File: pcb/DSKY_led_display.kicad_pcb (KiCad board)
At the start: 4 copper layers, 63.5 x 107.9 mm, 237 parts, among them J1 105133-0001, J2 20021221-00010C4LF, J3 TSM-104-01-L-SV, Q1 BSS138, Q2 BSS138, Q3 BSS138, Q4 BSS138, SW1 SWITCH_TACT_SMT4.6X2.8, U1 AP2204K-3.3, U2 LP5036, U3 LP5036, U4 LP5036, U5 LP5036, U6 ATSAMD21E18A-A, U7 LP5036, U8 LP5036

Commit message: V2 pcb as-ordered for testing
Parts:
- added C10: 1 uF, Capacitor_SMD:C_0603_1608Metric, F.Cu at (89.4, 128.4)
- added C11: 1 uF, Capacitor_SMD:C_0603_1608Metric, F.Cu at (64.1, 41.1)
- added C12: 1 uF, Capacitor_SMD:C_0603_1608Metric, F.Cu at (89.4, 109.0)
- added C13: 1 uF, Capacitor_SMD:C_0603_1608Metric, F.Cu at (43.9, 41.1)
- added C14: 1 uF, Capacitor_SMD:C_0603_1608Metric, F.Cu at (85.7, 41.1)
- added C9: 1 uF, Capacitor_SMD:C_0603_1608Metric, F.Cu at (89.5, 90.2)
- D191, D192: value D_Schottky -> B0540W
- R15, R16, R17, R18, R19, R20: value 3.7K -> 3.65K
- SW1: value SWITCH_TACT_SMT4.6X2.8 -> KMR241NG
- moved R15 57.2 mm to (92.7, 91.7), turned to 0 degrees
- moved C4 56.4 mm to (92.1, 95.5)
- moved C6 49.3 mm to (49.1, 38.1), turned to 0 degrees
- moved R6 45.3 mm to (46.1, 38.1), turned to 0 degrees
- moved R19 45.2 mm to (43.1, 38.1), turned to 180 degrees
- moved U2 43.5 mm to (85.1, 92.7), turned to 270 degrees
- moved U7 38.1 mm to (46.5, 45.6), turned to 0 degrees
- moved Q4 16.6 mm to (50.6, 75.2)
- moved Q3 16.6 mm to (57.0, 75.2)
- moved R11 16.6 mm to (57.1, 78.6)
- moved R13 16.6 mm to (50.6, 78.6)
- moved R14 16.6 mm to (50.6, 71.2)
- moved R12 16.6 mm to (57.0, 71.2)
- moved C3 13.4 mm to (92.3, 116.0), turned to 270 degrees
- moved J2 13.0 mm to (60.7, 53.7)
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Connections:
- U2 pad 45: +5V -> Net-(C9-Pad1)
- U3 pad 45: +5V -> Net-(C10-Pad1)
- U4 pad 45: +5V -> Net-(C12-Pad1)
- U5 pad 45: +5V -> Net-(C11-Pad1)
- U7 pad 45: +5V -> Net-(C13-Pad1)
- U8 pad 45: +5V -> Net-(C14-Pad1)
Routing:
- net GND: track 1070.7 -> 1396.6 mm, vias 9 -> 34
- net abus30: track 7.82 -> 63.9 mm
- net abus31: track 3.65 -> 58.1 mm
- net g5bus3: track 16.9 -> 69.9 mm, vias 1 -> 2
- net g5bus2: track 29.2 -> 79.5 mm, vias 2 -> 3
- net abus34: track 9.21 -> 59.2 mm
- net abus29: track 13.2 -> 60.2 mm
- net g5bus1: track 41.2 -> 88.0 mm, vias 2 -> 3
- net abus32: track 9.44 -> 55.2 mm
- net g6bus2: track 39.3 -> 84.2 mm, vias 1 -> 2
- net /EN0: track 173.9 -> 129.4 mm, vias 5 -> 6
- net g6bus3: track 36.6 -> 79.6 mm
- net abus33: track 11.6 -> 54.6 mm
- net g6bus1: track 51.6 -> 94.1 mm
- net abus0: track 52.5 -> 11.3 mm, vias 2 -> 1
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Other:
- net class Data: clearance 0.1 -> 0.15; trace_width 0.15 -> 0.2
- net class Default: clearance 0.1 -> 0.15; trace_width 0.15 -> 0.2
- net class GND added: clearance 0.15, trace_width 0.2, via_dia 0.6, via_drill 0.3
- net class Power: clearance 0.1 -> 0.15; trace_width 0.15 -> 0.2
- rule trace_clearance: 0.1 -> 0.15
- board text added: "+5V"
- board text added: "DSKY LED Display V2 Riley Rainey 2021-01-22"
- board text added: "GND"
- board text added: "N/C"
- board text added: "https://github.com/rrainey/DSKY-digital-indicator-replica"
- board text removed: "DSKY LED Display V1 Riley Rainey 2021-01-12"

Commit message: V3 board
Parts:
- removed Q1, Q2, Q3, Q4: BSS138, digikey-footprints:SOT-23-3
- removed R13, R14: 10K, Resistor_SMD:R_0603_1608Metric
- removed the REF** at (46.5, 110.7)
- added C15: 10 uF, Capacitor_SMD:C_0603_1608Metric, F.Cu at (52.2, 75.7)
- added REF**: OSHW-Logo2_24.3x20mm_SilkScreen, Symbol:OSHW-Logo2_24.3x20mm_SilkScreen, F.Cu at (48.7, 110.6)
- added U9: TCA9543ADR, Package_SO:SOIC-14_3.9x8.7mm_P1.27mm, F.Cu at (52.4, 81.0)
- J2: value 20021221-00010C4LF -> 3221-10-0300-00-TR
- R10, R7, R8, R9: value 10K -> 1K
- R11, R12: value 10K -> 4.7K
- moved R12 43.3 mm to (83.8, 37.1), turned to 180 degrees
- moved R11 39.6 mm to (93.7, 93.9), turned to 90 degrees
- moved R10 25.1 mm to (59.3, 83.1), turned to 270 degrees
- moved R8 24.3 mm to (46.7, 81.5), turned to 270 degrees
- moved R7 20.2 mm to (45.1, 83.1), turned to 270 degrees
- moved R9 16.1 mm to (57.7, 81.5), turned to 270 degrees
- moved R19 6.56 mm to (49.3, 40.1)
- moved R6 6.10 mm to (52.2, 38.3), turned to 90 degrees
- moved C13 5.40 mm to (49.3, 41.7)
- moved U7 5.33 mm to (51.8, 46.2)
- moved C6 4.66 mm to (53.8, 38.3), turned to 90 degrees
- moved R20 3.68 mm to (82.3, 40.2)
- moved C14 3.49 mm to (82.3, 41.8)
- moved R3 3.40 mm to (90.2, 135.9), turned to 270 degrees
- moved J2 3.28 mm to (60.7, 57.0)
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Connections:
- C1 pad 1: +5V -> VCC
- C2 pad 1: +5V -> VCC
- C3 pad 1: +5V -> VCC
- C4 pad 1: +5V -> VCC
- C6 pad 1: +5V -> VCC
- C7 pad 1: +5V -> VCC
- D191 pad 2: +5V -> VCC
- J3 pad 1: +5V -> VCC
- R1 pad 1: +5V -> VCC
- R10 pad 1: /EN1 -> VCC
- R10 pad 2: +5V -> /SDA1
- R11 pad 1: /3SDA -> VCC
- R11 pad 2: +3V3 -> Net-(R11-Pad2)
- R12 pad 1: /SDA -> VCC
- R12 pad 2: +5V -> Net-(R12-Pad2)
- R2 pad 1: +5V -> VCC
- R3 pad 1: +5V -> VCC
- R6 pad 1: +5V -> VCC
- R7 pad 1: /3EN0 -> VCC
- R7 pad 2: +3V3 -> /SCL0
- R8 pad 1: /EN0 -> VCC
- R8 pad 2: +5V -> /SDA0
- R9 pad 1: /3EN1 -> VCC
- R9 pad 2: +3V3 -> /SCL1
- U2 pad 40: +5V -> VCC
- U2 pad 41: /SDA -> /SDA0
- U2 pad 42: /SCL -> /SCL0
- U2 pad 43: /EN0 -> Net-(R11-Pad2)
- U3 pad 40: +5V -> VCC
- U3 pad 41: /SDA -> /SDA0
- U3 pad 42: /SCL -> /SCL0
- U3 pad 43: /EN0 -> Net-(R3-Pad2)
- U4 pad 40: +5V -> VCC
- U4 pad 41: /SDA -> /SDA0
- U4 pad 42: /SCL -> /SCL0
- U4 pad 43: /EN0 -> Net-(R1-Pad2)
- U5 pad 40: +5V -> VCC
- U5 pad 41: /SDA -> /SDA0
- U5 pad 42: /SCL -> /SCL0
- U5 pad 43: /EN0 -> Net-(R2-Pad2)
- U6 pad 1: /3EN0 -> Net-(U6-Pad1)
- U6 pad 2: /3EN1 -> Net-(U6-Pad2)
- U6 pad 22: /D- -> Net-(U6-Pad22)
- U6 pad 23: /D+ -> /D-
- U6 pad 24: Net-(U6-Pad24) -> /D+
- U6 pad 3: Net-(U6-Pad3) -> /BRESET
- U7 pad 40: +5V -> VCC
- U7 pad 41: /SDA -> /SDA1
- U7 pad 42: /SCL -> /SCL1
- U7 pad 43: /EN1 -> Net-(R6-Pad2)
- U8 pad 40: +5V -> VCC
- U8 pad 41: /SDA -> /SDA1
- U8 pad 42: /SCL -> /SCL1
- U8 pad 43: /EN1 -> Net-(R12-Pad2)
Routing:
- net +5V: track 244.6 -> 0.00 mm, vias 5 -> 0
- net VCC: track 0.00 -> 226.6 mm, vias 0 -> 5
- net /SCL: track 200.0 -> 0.00 mm, vias 7 -> 0
- net /SDA: track 188.3 -> 0.00 mm, vias 7 -> 0
- net GND: track 1396.6 -> 1226.0 mm, vias 34 -> 7
- net /SDA0: track 0.00 -> 139.3 mm, vias 0 -> 5
- net /SCL0: track 0.00 -> 138.4 mm, vias 0 -> 5
- net /EN0: track 129.4 -> 0.00 mm, vias 6 -> 0
- net /SCL1: track 0.00 -> 93.7 mm, vias 0 -> 3
- net /SDA1: track 0.00 -> 88.1 mm, vias 0 -> 3
- net /EN1: track 69.9 -> 0.00 mm, vias 3 -> 0
- net cbus7: track 37.4 -> 14.1 mm, vias 2 -> 1
- net g5bus1: track 88.0 -> 67.9 mm, vias 3 -> 2
- net g5bus0: track 92.9 -> 74.4 mm
- net abus7: track 32.1 -> 13.6 mm, vias 2 -> 1
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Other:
- net class VCC added: clearance 0.15, trace_width 0.45, via_dia 0.6, via_drill 0.3
- board text added: "+3.3V"
- board text added: "DSKY LED Display V3 Riley Rainey 2021-02-23"
- board text removed: "+5V"
- board text removed: "DSKY LED Display V2 Riley Rainey 2021-01-22"

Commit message: V4 board
Version 4 of the PCB
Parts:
- removed R1, R11, R12, R2, R3, R6: 4.7K, Resistor_SMD:R_0603_1608Metric
- added R13: 0K, Resistor_SMD:R_0603_1608Metric, F.Cu at (59.2, 66.5)
- added R14: 1K, Resistor_SMD:R_0603_1608Metric, F.Cu at (59.5, 74.0)
- added R21: 1K, Resistor_SMD:R_0603_1608Metric, F.Cu at (57.8, 74.0)
- added R22: 1K, Resistor_SMD:R_0603_1608Metric, F.Cu at (43.3, 81.5)
- added R23: 1K, Resistor_SMD:R_0603_1608Metric, F.Cu at (59.3, 86.6)
- moved C1 3.71 mm to (90.7, 132.4), turned to 0 degrees
- moved C3 3.55 mm to (90.7, 112.8), turned to 0 degrees
- moved R17 3.53 mm to (91.0, 109.0)
- moved R16 2.69 mm to (91.0, 128.4)
- moved R15 2.61 mm to (91.1, 90.2)
- moved C4 2.46 mm to (90.3, 93.8), turned to 0 degrees
- moved R7 1.60 mm to (45.0, 81.5)
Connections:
- D10 pad 1: GND -> g0bus1
- D10 pad 2: g0bus1 -> VCC
- D100 pad 1: GND -> abus32
- D100 pad 2: abus32 -> VCC
- D101 pad 1: GND -> abus3
- D101 pad 2: abus3 -> VCC
- D102 pad 1: GND -> sabus2
- D102 pad 2: sabus2 -> VCC
- D103 pad 1: GND -> abus10
- D103 pad 2: abus10 -> VCC
- D104 pad 1: GND -> abus17
- D104 pad 2: abus17 -> VCC
- D105 pad 1: GND -> abus24
- D105 pad 2: abus24 -> VCC
- D106 pad 1: GND -> abus31
- D106 pad 2: abus31 -> VCC
- D107 pad 1: GND -> g5bus0
- D107 pad 2: g5bus0 -> VCC
- D108 pad 1: GND -> g5bus1
- D108 pad 2: g5bus1 -> VCC
- D109 pad 1: GND -> g5bus2
- D109 pad 2: g5bus2 -> VCC
- D11 pad 1: GND -> g0bus6
- D11 pad 2: g0bus6 -> VCC
- D110 pad 1: GND -> g5bus3
- D110 pad 2: g5bus3 -> VCC
- D111 pad 1: GND -> bbus0
- D111 pad 2: bbus0 -> VCC
- D112 pad 1: GND -> sbbus0
- D112 pad 2: sbbus0 -> VCC
- D113 pad 1: GND -> bbus7
- D113 pad 2: bbus7 -> VCC
- D114 pad 1: GND -> bbus14
- D114 pad 2: bbus14 -> VCC
- D115 pad 1: GND -> bbus21
- D115 pad 2: bbus21 -> VCC
- D116 pad 1: GND -> bbus28
- D116 pad 2: bbus28 -> VCC
- D117 pad 1: GND -> bbus5
- D117 pad 2: bbus5 -> VCC
- D118 pad 1: GND -> bbus1
- D118 pad 2: bbus1 -> VCC
- D119 pad 1: GND -> bbus12
- D119 pad 2: bbus12 -> VCC
- D12 pad 1: GND -> g0bus5
- D12 pad 2: g0bus5 -> VCC
- D120 pad 1: GND -> bbus19
- D120 pad 2: bbus19 -> VCC
- D121 pad 1: GND -> bbus8
- D121 pad 2: bbus8 -> VCC
- D122 pad 1: GND -> bbus15
- D122 pad 2: bbus15 -> VCC
- D123 pad 1: GND -> bbus26
- D123 pad 2: bbus26 -> VCC
- D124 pad 1: GND -> bbus33
- D124 pad 2: bbus33 -> VCC
- D125 pad 1: GND -> bbus22
- D125 pad 2: bbus22 -> VCC
- D126 pad 1: GND -> bbus29
- D126 pad 2: bbus29 -> VCC
- D127 pad 1: GND -> sbbus1
- D127 pad 2: sbbus1 -> VCC
- D128 pad 1: GND -> bbus6
- D128 pad 2: bbus6 -> VCC
- D129 pad 1: GND -> bbus13
- D129 pad 2: bbus13 -> VCC
- D13 pad 1: GND -> g0bus4
- D13 pad 2: g0bus4 -> VCC
- D130 pad 1: GND -> bbus20
- D130 pad 2: bbus20 -> VCC
- D131 pad 1: GND -> bbus27
- D131 pad 2: bbus27 -> VCC
- D132 pad 1: GND -> bbus34
- D132 pad 2: bbus34 -> VCC
- D133 pad 1: GND -> bbus2
- D133 pad 2: bbus2 -> VCC
- D134 pad 1: GND -> bbus4
- D134 pad 2: bbus4 -> VCC
- D135 pad 1: GND -> bbus9
- D135 pad 2: bbus9 -> VCC
- D136 pad 1: GND -> bbus16
- D136 pad 2: bbus16 -> VCC
- D137 pad 1: GND -> bbus11
- D137 pad 2: bbus11 -> VCC
- D138 pad 1: GND -> bbus18
- D138 pad 2: bbus18 -> VCC
- D139 pad 1: GND -> bbus23
- D139 pad 2: bbus23 -> VCC
- D14 pad 1: GND -> g0bus7
- D14 pad 2: g0bus7 -> VCC
- D140 pad 1: GND -> bbus30
- D140 pad 2: bbus30 -> VCC
- D141 pad 1: GND -> bbus25
- D141 pad 2: bbus25 -> VCC
- D142 pad 1: GND -> bbus32
- D142 pad 2: bbus32 -> VCC
- D143 pad 1: GND -> sbbus2
- D143 pad 2: sbbus2 -> VCC
- D144 pad 1: GND -> bbus3
- D144 pad 2: bbus3 -> VCC
- D145 pad 1: GND -> bbus10
- D145 pad 2: bbus10 -> VCC
- D146 pad 1: GND -> bbus17
- D146 pad 2: bbus17 -> VCC
- D147 pad 1: GND -> bbus24
- D147 pad 2: bbus24 -> VCC
- D148 pad 1: GND -> bbus31
- D148 pad 2: bbus31 -> VCC
- D149 pad 1: GND -> g6bus0
- D149 pad 2: g6bus0 -> VCC
- D15 pad 1: GND -> dbus0
- D15 pad 2: dbus0 -> VCC
- D150 pad 1: GND -> g6bus1
- D150 pad 2: g6bus1 -> VCC
- D151 pad 1: GND -> g6bus2
- D151 pad 2: g6bus2 -> VCC
- D152 pad 1: GND -> g6bus3
- D152 pad 2: g6bus3 -> VCC
- D153 pad 1: GND -> scbus0
- D153 pad 2: scbus0 -> VCC
- D154 pad 1: GND -> cbus0
- D154 pad 2: cbus0 -> VCC
- D155 pad 1: GND -> cbus7
- D155 pad 2: cbus7 -> VCC
- D156 pad 1: GND -> cbus14
- D156 pad 2: cbus14 -> VCC
- D157 pad 1: GND -> cbus21
- D157 pad 2: cbus21 -> VCC
- D158 pad 1: GND -> cbus28
- D158 pad 2: cbus28 -> VCC
- D159 pad 1: GND -> cbus5
- D159 pad 2: cbus5 -> VCC
- D16 pad 1: GND -> dbus7
- D16 pad 2: dbus7 -> VCC
- D160 pad 1: GND -> cbus1
- D160 pad 2: cbus1 -> VCC
- D161 pad 1: GND -> cbus12
- D161 pad 2: cbus12 -> VCC
- D162 pad 1: GND -> cbus19
- D162 pad 2: cbus19 -> VCC
- D163 pad 1: GND -> scbus1
- D163 pad 2: scbus1 -> VCC
- D164 pad 1: GND -> cbus8
- D164 pad 2: cbus8 -> VCC
- D165 pad 1: GND -> cbus15
- D165 pad 2: cbus15 -> VCC
- D166 pad 1: GND -> cbus26
- D166 pad 2: cbus26 -> VCC
- D167 pad 1: GND -> cbus33
- D167 pad 2: cbus33 -> VCC
- D168 pad 1: GND -> cbus22
- D168 pad 2: cbus22 -> VCC
- D169 pad 1: GND -> cbus29
- D169 pad 2: cbus29 -> VCC
- D17 pad 1: GND -> dbus5
- D17 pad 2: dbus5 -> VCC
- D170 pad 1: GND -> cbus6
- D170 pad 2: cbus6 -> VCC
- D171 pad 1: GND -> cbus13
- D171 pad 2: cbus13 -> VCC
- D172 pad 1: GND -> cbus20
- D172 pad 2: cbus20 -> VCC
- D173 pad 1: GND -> cbus27
- D173 pad 2: cbus27 -> VCC
- D174 pad 1: GND -> cbus34
- D174 pad 2: cbus34 -> VCC
- D175 pad 1: GND -> cbus2
- D175 pad 2: cbus2 -> VCC
- D176 pad 1: GND -> scbus2
- D176 pad 2: scbus2 -> VCC
- D177 pad 1: GND -> cbus4
- D177 pad 2: cbus4 -> VCC
- D178 pad 1: GND -> cbus9
- D178 pad 2: cbus9 -> VCC
- D179 pad 1: GND -> cbus16
- D179 pad 2: cbus16 -> VCC
- D18 pad 1: GND -> dbus12
- D18 pad 2: dbus12 -> VCC
- D180 pad 1: GND -> cbus11
- D180 pad 2: cbus11 -> VCC
- D181 pad 1: GND -> cbus18
- D181 pad 2: cbus18 -> VCC
- D182 pad 1: GND -> cbus23
- D182 pad 2: cbus23 -> VCC
- D183 pad 1: GND -> cbus30
- D183 pad 2: cbus30 -> VCC
- D184 pad 1: GND -> cbus25
- D184 pad 2: cbus25 -> VCC
- D185 pad 1: GND -> cbus32
- D185 pad 2: cbus32 -> VCC
- D186 pad 1: GND -> cbus3
- D186 pad 2: cbus3 -> VCC
- D187 pad 1: GND -> cbus10
- D187 pad 2: cbus10 -> VCC
- D188 pad 1: GND -> cbus17
- D188 pad 2: cbus17 -> VCC
- D189 pad 1: GND -> cbus24
- D189 pad 2: cbus24 -> VCC
- D19 pad 1: GND -> dbus1
- D19 pad 2: dbus1 -> VCC
- D190 pad 1: GND -> cbus31
- D190 pad 2: cbus31 -> VCC
- D20 pad 1: GND -> dbus8
- D20 pad 2: dbus8 -> VCC
- D21 pad 1: GND -> dbus6
- D21 pad 2: dbus6 -> VCC
- D22 pad 1: GND -> dbus13
- D22 pad 2: dbus13 -> VCC
- D23 pad 1: GND -> dbus2
- D23 pad 2: dbus2 -> VCC
- D24 pad 1: GND -> dbus9
- D24 pad 2: dbus9 -> VCC
- D25 pad 1: GND -> dbus4
- D25 pad 2: dbus4 -> VCC
- D26 pad 1: GND -> dbus11
- D26 pad 2: dbus11 -> VCC
- D27 pad 1: GND -> dbus3
- D27 pad 2: dbus3 -> VCC
- D28 pad 1: GND -> dbus10
- D28 pad 2: dbus10 -> VCC
- D29 pad 1: GND -> g2bus0
- D29 pad 2: g2bus0 -> VCC
- D3 pad 1: GND -> g0bus0
- D3 pad 2: g0bus0 -> VCC
- D30 pad 1: GND -> g2bus3
- D30 pad 2: g2bus3 -> VCC
- D31 pad 1: GND -> g3bus0
- D31 pad 2: g3bus0 -> VCC
- D32 pad 1: GND -> g3bus3
- D32 pad 2: g3bus3 -> VCC
- D33 pad 1: GND -> g2bus1
- D33 pad 2: g2bus1 -> VCC
- D34 pad 1: GND -> g2bus2
- D34 pad 2: g2bus2 -> VCC
- D35 pad 1: GND -> g3bus1
- D35 pad 2: g3bus1 -> VCC
- D36 pad 1: GND -> g3bus2
- D36 pad 2: g3bus2 -> VCC
- D37 pad 1: GND -> ebus0
- D37 pad 2: ebus0 -> VCC
- D38 pad 1: GND -> ebus7
- D38 pad 2: ebus7 -> VCC
- D39 pad 1: GND -> fbus0
- D39 pad 2: fbus0 -> VCC
- D4 pad 1: GND -> g0bus2
- D4 pad 2: g0bus2 -> VCC
- D40 pad 1: GND -> fbus7
- D40 pad 2: fbus7 -> VCC
- D41 pad 1: GND -> ebus5
- D41 pad 2: ebus5 -> VCC
- D42 pad 1: GND -> ebus12
- D42 pad 2: ebus12 -> VCC
- D43 pad 1: GND -> ebus1
- D43 pad 2: ebus1 -> VCC
- D44 pad 1: GND -> ebus8
- D44 pad 2: ebus8 -> VCC
- D45 pad 1: GND -> fbus5
- D45 pad 2: fbus5 -> VCC
- D46 pad 1: GND -> fbus12
- D46 pad 2: fbus12 -> VCC
- D47 pad 1: GND -> fbus1
- D47 pad 2: fbus1 -> VCC
- D48 pad 1: GND -> fbus8
- D48 pad 2: fbus8 -> VCC
- D49 pad 1: GND -> ebus6
- D49 pad 2: ebus6 -> VCC
- D5 pad 1: GND -> g1bus0
- D5 pad 2: g1bus0 -> VCC
- D50 pad 1: GND -> ebus13
- D50 pad 2: ebus13 -> VCC
- D51 pad 1: GND -> fbus6
- D51 pad 2: fbus6 -> VCC
- D52 pad 1: GND -> fbus13
- D52 pad 2: fbus13 -> VCC
- D53 pad 1: GND -> ebus2
- D53 pad 2: ebus2 -> VCC
- D54 pad 1: GND -> ebus9
- D54 pad 2: ebus9 -> VCC
- D55 pad 1: GND -> ebus4
- D55 pad 2: ebus4 -> VCC
- D56 pad 1: GND -> VCC
- D57 pad 1: GND -> fbus2
- D57 pad 2: fbus2 -> VCC
- D58 pad 1: GND -> fbus9
- D58 pad 2: fbus9 -> VCC
- D59 pad 1: GND -> fbus4
- D59 pad 2: fbus4 -> VCC
- D6 pad 1: GND -> g1bus3
- D6 pad 2: g1bus3 -> VCC
- D60 pad 1: GND -> fbus11
- D60 pad 2: fbus11 -> VCC
- D61 pad 1: GND -> ebus3
- D61 pad 2: ebus3 -> VCC
- D62 pad 1: GND -> ebus10
- D62 pad 2: ebus10 -> VCC
- D63 pad 1: GND -> fbus3
- D63 pad 2: fbus3 -> VCC
- D64 pad 1: GND -> fbus10
- D64 pad 2: fbus10 -> VCC
- D65 pad 1: GND -> g4bus0
- D65 pad 2: g4bus0 -> VCC
- D66 pad 1: GND -> g4bus1
- D66 pad 2: g4bus1 -> VCC
- D67 pad 1: GND -> g4bus2
- D67 pad 2: g4bus2 -> VCC
- D68 pad 1: GND -> g4bus3
- D68 pad 2: g4bus3 -> VCC
- D69 pad 1: GND -> abus0
- D69 pad 2: abus0 -> VCC
- D7 pad 1: GND -> g0bus3
- D7 pad 2: g0bus3 -> VCC
- D70 pad 1: GND -> abus7
- D70 pad 2: abus7 -> VCC
- D71 pad 1: GND -> abus14
- D71 pad 2: abus14 -> VCC
- D72 pad 1: GND -> abus21
- D72 pad 2: abus21 -> VCC
- D73 pad 1: GND -> abus28
- D73 pad 2: abus28 -> VCC
- D74 pad 1: GND -> sabus0
- D74 pad 2: sabus0 -> VCC
- D75 pad 1: GND -> abus5
- D75 pad 2: abus5 -> VCC
- D76 pad 1: GND -> abus1
- D76 pad 2: abus1 -> VCC
- D77 pad 1: GND -> abus12
- D77 pad 2: abus12 -> VCC
- D78 pad 1: GND -> abus19
- D78 pad 2: abus19 -> VCC
- D79 pad 1: GND -> abus8
- D79 pad 2: abus8 -> VCC
- D8 pad 1: GND -> g1bus1
- D8 pad 2: g1bus1 -> VCC
- D80 pad 1: GND -> abus15
- D80 pad 2: abus15 -> VCC
- D81 pad 1: GND -> abus26
- D81 pad 2: abus26 -> VCC
- D82 pad 1: GND -> abus33
- D82 pad 2: abus33 -> VCC
- D83 pad 1: GND -> abus22
- D83 pad 2: abus22 -> VCC
- D84 pad 1: GND -> abus29
- D84 pad 2: abus29 -> VCC
- D85 pad 1: GND -> abus6
- D85 pad 2: abus6 -> VCC
- D86 pad 1: GND -> sabus1
- D86 pad 2: sabus1 -> VCC
- D87 pad 1: GND -> abus13
- D87 pad 2: abus13 -> VCC
- D88 pad 1: GND -> abus20
- D88 pad 2: abus20 -> VCC
- D89 pad 1: GND -> abus27
- D89 pad 2: abus27 -> VCC
- D9 pad 1: GND -> g1bus2
- D9 pad 2: g1bus2 -> VCC
- D90 pad 1: GND -> abus34
- D90 pad 2: abus34 -> VCC
- D91 pad 1: GND -> abus2
- D91 pad 2: abus2 -> VCC
- D92 pad 1: GND -> abus4
- D92 pad 2: abus4 -> VCC
- D93 pad 1: GND -> abus9
- D93 pad 2: abus9 -> VCC
- D94 pad 1: GND -> abus16
- D94 pad 2: abus16 -> VCC
- D95 pad 1: GND -> abus11
- D95 pad 2: abus11 -> VCC
- D96 pad 1: GND -> abus18
- D96 pad 2: abus18 -> VCC
- D97 pad 1: GND -> abus23
- D97 pad 2: abus23 -> VCC
- D98 pad 1: GND -> abus30
- D98 pad 2: abus30 -> VCC
- D99 pad 1: GND -> abus25
- D99 pad 2: abus25 -> VCC
- J1 pad 4: Net-(J1-Pad4) -> (no net)
- J1 pad S2: Net-(J1-PadS2) -> (no net)
- J2 pad 10: Net-(J2-Pad10) -> (no net)
- J2 pad 6: Net-(J2-Pad6) -> (no net)
- J2 pad 7: Net-(J2-Pad7) -> (no net)
- J2 pad 8: Net-(J2-Pad8) -> (no net)
- J3 pad 2: Net-(J3-Pad2) -> (no net)
- J3 pad 4: Net-(J3-Pad4) -> (no net)
- U1 pad 4: Net-(U1-Pad4) -> (no net)
- U2 pad 36: Net-(U2-Pad36) -> (no net)
- U2 pad 43: Net-(R11-Pad2) -> VCC
- U3 pad 36: Net-(U3-Pad36) -> (no net)
- U3 pad 39: Net-(R3-Pad2) -> VCC
- U3 pad 43: Net-(R3-Pad2) -> VCC
- U4 pad 36: Net-(U4-Pad36) -> (no net)
- U4 pad 38: Net-(R1-Pad2) -> VCC
- U4 pad 43: Net-(R1-Pad2) -> VCC
- U5 pad 38: Net-(R2-Pad2) -> VCC
- U5 pad 39: Net-(R2-Pad2) -> VCC
- U5 pad 43: Net-(R2-Pad2) -> VCC
- U6 pad 1: Net-(U6-Pad1) -> /BRESET
- U6 pad 14: Net-(U6-Pad14) -> (no net)
- U6 pad 15: Net-(U6-Pad15) -> (no net)
- U6 pad 16: Net-(U6-Pad16) -> (no net)
- U6 pad 17: Net-(U6-Pad17) -> (no net)
- U6 pad 18: Net-(U6-Pad18) -> (no net)
- U6 pad 19: Net-(U6-Pad19) -> (no net)
- U6 pad 2: Net-(U6-Pad2) -> (no net)
- U6 pad 20: Net-(U6-Pad20) -> (no net)
- U6 pad 21: Net-(U6-Pad21) -> (no net)
- U6 pad 22: Net-(U6-Pad22) -> (no net)
- U6 pad 25: Net-(U6-Pad25) -> (no net)
- U6 pad 27: Net-(U6-Pad27) -> (no net)
- U6 pad 3: /BRESET -> (no net)
- U6 pad 4: Net-(U6-Pad4) -> (no net)
- U6 pad 5: Net-(U6-Pad5) -> (no net)
- U6 pad 6: Net-(U6-Pad6) -> (no net)
- U6 pad 7: Net-(U6-Pad7) -> (no net)
- U6 pad 8: Net-(U6-Pad8) -> (no net)
- U7 pad 13: Net-(U7-Pad13) -> (no net)
- U7 pad 14: Net-(U7-Pad14) -> (no net)
- U7 pad 15: Net-(U7-Pad15) -> (no net)
- U7 pad 16: Net-(U7-Pad16) -> (no net)
- U7 pad 17: Net-(U7-Pad17) -> (no net)
- U7 pad 18: Net-(U7-Pad18) -> (no net)
- U7 pad 19: Net-(U7-Pad19) -> (no net)
- U7 pad 20: Net-(U7-Pad20) -> (no net)
- U7 pad 21: Net-(U7-Pad21) -> (no net)
- U7 pad 22: Net-(U7-Pad22) -> (no net)
- U7 pad 23: Net-(U7-Pad23) -> (no net)
- U7 pad 24: Net-(U7-Pad24) -> (no net)
- U7 pad 25: Net-(U7-Pad25) -> (no net)
- U7 pad 26: Net-(U7-Pad26) -> (no net)
- U7 pad 27: Net-(U7-Pad27) -> (no net)
- U7 pad 28: Net-(U7-Pad28) -> (no net)
- U7 pad 29: Net-(U7-Pad29) -> (no net)
- U7 pad 30: Net-(U7-Pad30) -> (no net)
- U7 pad 31: Net-(U7-Pad31) -> (no net)
- U7 pad 32: Net-(U7-Pad32) -> (no net)
- U7 pad 33: Net-(U7-Pad33) -> (no net)
- U7 pad 34: Net-(U7-Pad34) -> (no net)
- U7 pad 35: Net-(U7-Pad35) -> (no net)
- U7 pad 36: Net-(U7-Pad36) -> (no net)
- U7 pad 38: Net-(R6-Pad2) -> VCC
- U7 pad 43: Net-(R6-Pad2) -> VCC
- U8 pad 36: Net-(U8-Pad36) -> (no net)
- U8 pad 43: Net-(R12-Pad2) -> VCC
- U9 pad 11: Net-(U9-Pad11) -> (no net)
- U9 pad 12: /3SDA -> /3SCL
- U9 pad 13: /3SCL -> /3SDA
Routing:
- net GND: track 1226.0 -> 300.1 mm, vias 7 -> 8
- net VCC: track 226.6 -> 1083.5 mm, vias 5 -> 7
- net fbus0: track 44.5 -> 64.6 mm, vias 1 -> 2
- net g4bus0: track 79.5 -> 60.1 mm
- net /SCL0: track 138.4 -> 155.7 mm, vias 5 -> 3
- net abus28: track 65.0 -> 51.0 mm
- net Net-(R12-Pad2): track 12.0 -> 0.00 mm
- net Net-(R6-Pad2): track 11.6 -> 0.00 mm, vias 3 -> 0
- net dbus6: track 14.2 -> 25.7 mm, vias 1 -> 2
- net cbus17: track 19.7 -> 30.8 mm
- net ebus4: track 55.2 -> 44.3 mm, vias 2 -> 3
- net g4bus1: track 57.5 -> 47.1 mm
- net fbus10: track 56.8 -> 66.1 mm
- net fbus4: track 54.7 -> 45.4 mm
- net /SCL1: track 93.7 -> 85.1 mm
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- added copper zone on In1.Cu, net GND
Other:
- board text added: "DSKY LED Display V4 Riley Rainey 2021-08-01"
- board text removed: "DSKY LED Display V3 Riley Rainey 2021-02-23"

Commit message: V4 PCB update
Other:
- board size 63.5 x 107.9 mm -> 63.5 x 105.5 mm
- board text added: "DSKY LED Display V5 Riley Rainey 2021-09-01"
- board text removed: "DSKY LED Display V4 Riley Rainey 2021-08-01"

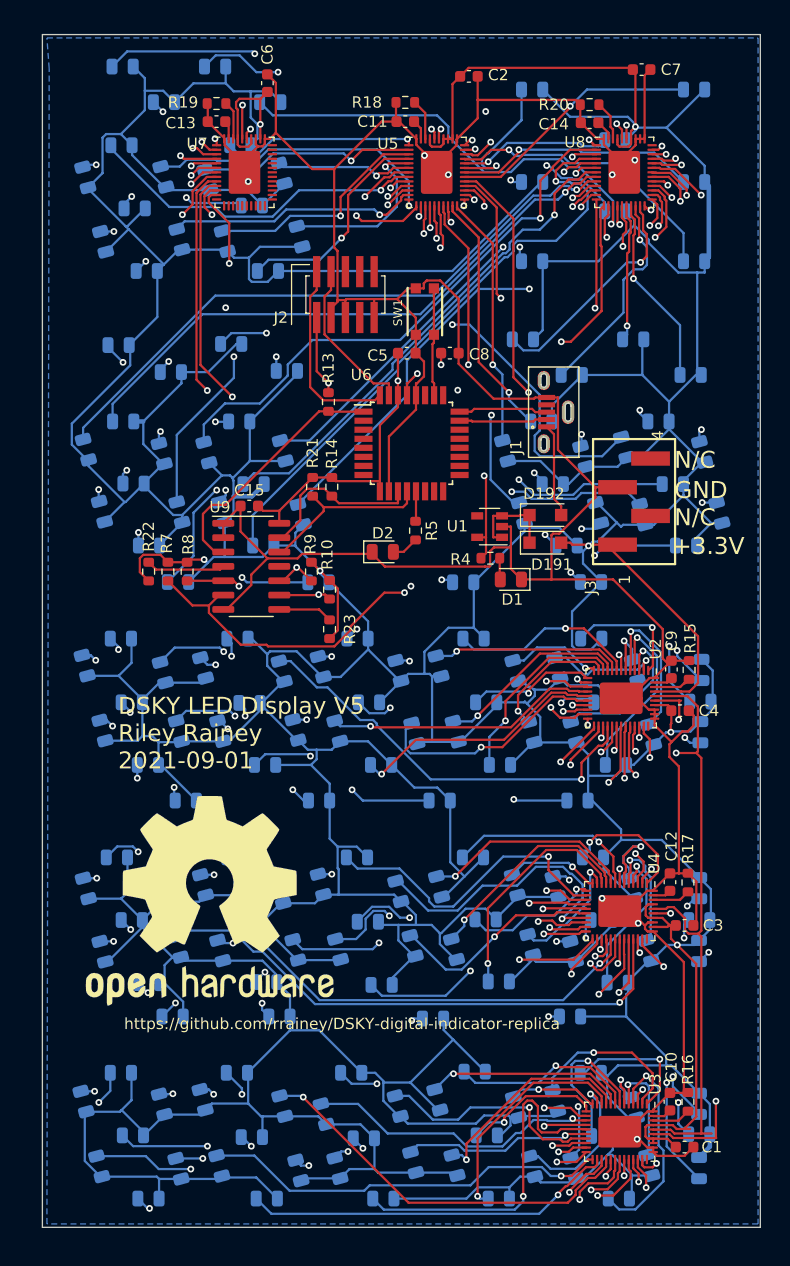
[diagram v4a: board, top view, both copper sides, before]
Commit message: V7 PCB fixes placement of D56 LED -- it was reversed.
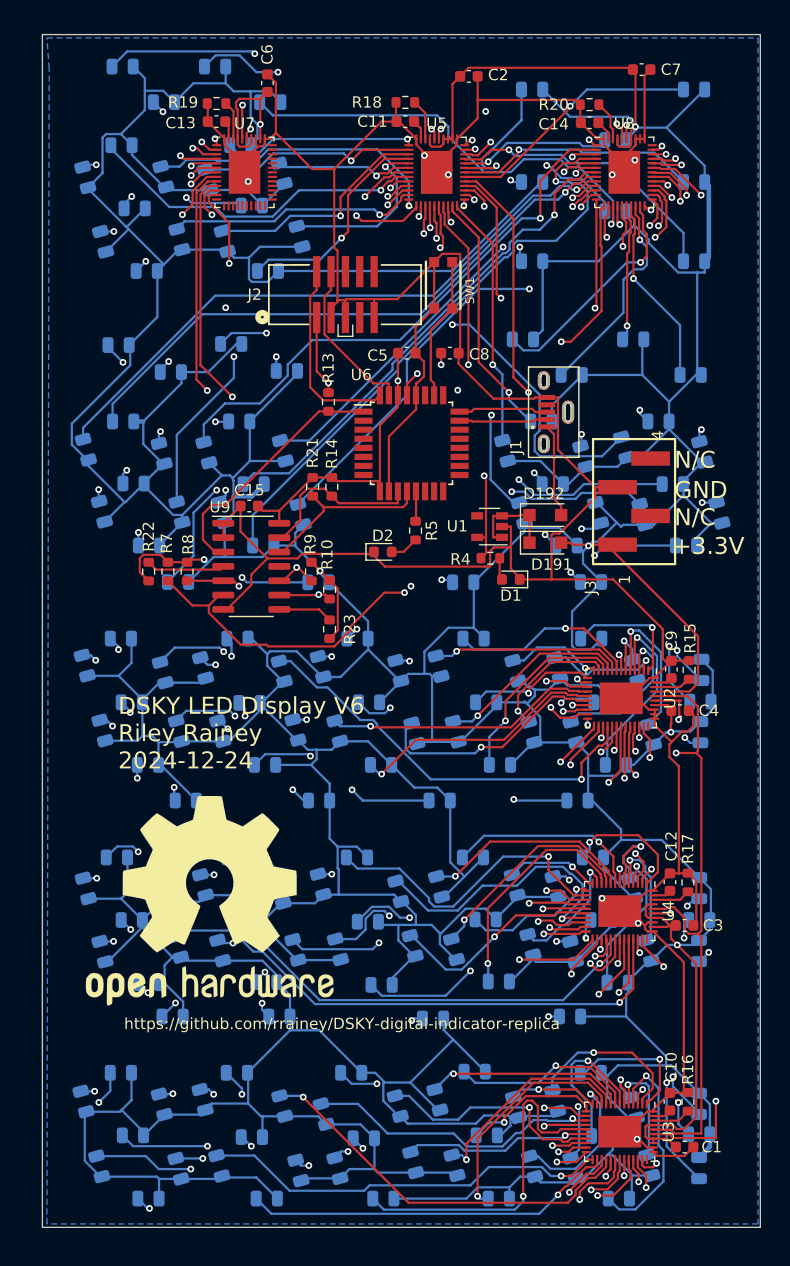
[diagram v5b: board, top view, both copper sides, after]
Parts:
- D1, D2: footprint LED_SMD:LED_0805_2012Metric -> LED_SMD:LED_0603_1608Metric
- U2, U3, U4, U5, U7, U8: footprint Package_DFN_QFN:VQFN-46-1EP_5x6mm_P0.4mm_EP2.8x3.8mm -> led-project:VQFN-46-optimized
- moved SW1 2.84 mm to (69.3, 56.2)
- turned D56 to 105 degrees
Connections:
- net sabus0 renamed /sabus0
- net sabus1 renamed /sabus1
- net sabus2 renamed /sabus2
- net sbbus0 renamed /sbbus0
- net sbbus1 renamed /sbbus1
- net sbbus2 renamed /sbbus2
- net scbus0 renamed /scbus0
- net scbus1 renamed /scbus1
- net scbus2 renamed /scbus2
- D56 pad 1: VCC -> ebus11
- D56 pad 2: ebus11 -> VCC
- J1 pad 4: (no net) -> unconnected-(J1-ID-Pad4)
- J1 pad S2: (no net) -> unconnected-(J1-SHIELD-PadS2)
- J2 pad 10: (no net) -> unconnected-(J2-Pad10)
- J2 pad 6: (no net) -> unconnected-(J2-Pad6)
- J2 pad 7: (no net) -> unconnected-(J2-Pad7)
- J2 pad 8: (no net) -> unconnected-(J2-Pad8)
- J3 pad 2: (no net) -> unconnected-(J3-Pad2)
- J3 pad 4: (no net) -> unconnected-(J3-Pad4)
- U1 pad 4: (no net) -> unconnected-(U1-NC-Pad4)
- U2 pad 36: (no net) -> unconnected-(U2-OUT35-Pad36)
- U3 pad 36: (no net) -> unconnected-(U3-OUT35-Pad36)
- U4 pad 36: (no net) -> unconnected-(U4-OUT35-Pad36)
- U6 pad 14: (no net) -> unconnected-(U6-PA11-Pad14)
- U6 pad 15: (no net) -> unconnected-(U6-PA14-Pad15)
- U6 pad 16: (no net) -> unconnected-(U6-PA15-Pad16)
- U6 pad 17: (no net) -> unconnected-(U6-PA16-Pad17)
- U6 pad 18: (no net) -> unconnected-(U6-PA17-Pad18)
- U6 pad 19: (no net) -> unconnected-(U6-PA18-Pad19)
- U6 pad 2: (no net) -> unconnected-(U6-PA01-Pad2)
- U6 pad 20: (no net) -> unconnected-(U6-PA19-Pad20)
- U6 pad 21: (no net) -> unconnected-(U6-PA22-Pad21)
- U6 pad 22: (no net) -> unconnected-(U6-PA23-Pad22)
- U6 pad 25: (no net) -> unconnected-(U6-PA27-Pad25)
- U6 pad 27: (no net) -> unconnected-(U6-PA28-Pad27)
- U6 pad 3: (no net) -> unconnected-(U6-PA02-Pad3)
- U6 pad 4: (no net) -> unconnected-(U6-PA03-Pad4)
- U6 pad 5: (no net) -> unconnected-(U6-PA04-Pad5)
- U6 pad 6: (no net) -> unconnected-(U6-PA05-Pad6)
- U6 pad 7: (no net) -> unconnected-(U6-PA06-Pad7)
- U6 pad 8: (no net) -> unconnected-(U6-PA07-Pad8)
- U7 pad 13: (no net) -> unconnected-(U7-OUT12-Pad13)
- U7 pad 14: (no net) -> unconnected-(U7-OUT13-Pad14)
- U7 pad 15: (no net) -> unconnected-(U7-OUT14-Pad15)
- U7 pad 16: (no net) -> unconnected-(U7-OUT15-Pad16)
- U7 pad 17: (no net) -> unconnected-(U7-OUT16-Pad17)
- U7 pad 18: (no net) -> unconnected-(U7-OUT17-Pad18)
- U7 pad 19: (no net) -> unconnected-(U7-OUT18-Pad19)
- U7 pad 20: (no net) -> unconnected-(U7-OUT19-Pad20)
- U7 pad 21: (no net) -> unconnected-(U7-OUT20-Pad21)
- U7 pad 22: (no net) -> unconnected-(U7-OUT21-Pad22)
- U7 pad 23: (no net) -> unconnected-(U7-OUT22-Pad23)
- U7 pad 24: (no net) -> unconnected-(U7-OUT23-Pad24)
- U7 pad 25: (no net) -> unconnected-(U7-OUT24-Pad25)
- U7 pad 26: (no net) -> unconnected-(U7-OUT25-Pad26)
- U7 pad 27: (no net) -> unconnected-(U7-OUT26-Pad27)
- U7 pad 28: (no net) -> unconnected-(U7-OUT27-Pad28)
- U7 pad 29: (no net) -> unconnected-(U7-OUT28-Pad29)
- U7 pad 30: (no net) -> unconnected-(U7-OUT29-Pad30)
- U7 pad 31: (no net) -> unconnected-(U7-OUT30-Pad31)
- U7 pad 32: (no net) -> unconnected-(U7-OUT31-Pad32)
- U7 pad 33: (no net) -> unconnected-(U7-OUT32-Pad33)
- U7 pad 34: (no net) -> unconnected-(U7-OUT33-Pad34)
- U7 pad 35: (no net) -> unconnected-(U7-OUT34-Pad35)
- U7 pad 36: (no net) -> unconnected-(U7-OUT35-Pad36)
- U8 pad 36: (no net) -> unconnected-(U8-OUT35-Pad36)
- U9 pad 11: (no net) -> unconnected-(U9-INT-Pad11)
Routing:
- net GND: track 300.1 -> 307.6 mm
- net Net-(SW1-S): track 9.56 -> 12.7 mm
- net /SCL0: track 155.7 -> 154.8 mm
- net VCC: track 1083.5 -> 1082.9 mm
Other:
- net class Data removed
- net class Default removed
- net class GND removed
- net class Power removed
- net class VCC removed
- board text added: "DSKY LED Display V6 Riley Rainey 2024-12-24"
- board text removed: "DSKY LED Display V5 Riley Rainey 2021-09-01"
